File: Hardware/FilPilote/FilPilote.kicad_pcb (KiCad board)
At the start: 2 copper layers, 50 x 40 mm, 15 parts, among them J1 Conn_01x04_Male, P1 CONN_01X03, U1 MOC3041M, U2 MOC3041M, U4 ESP-12E, U5 HLK-PM03

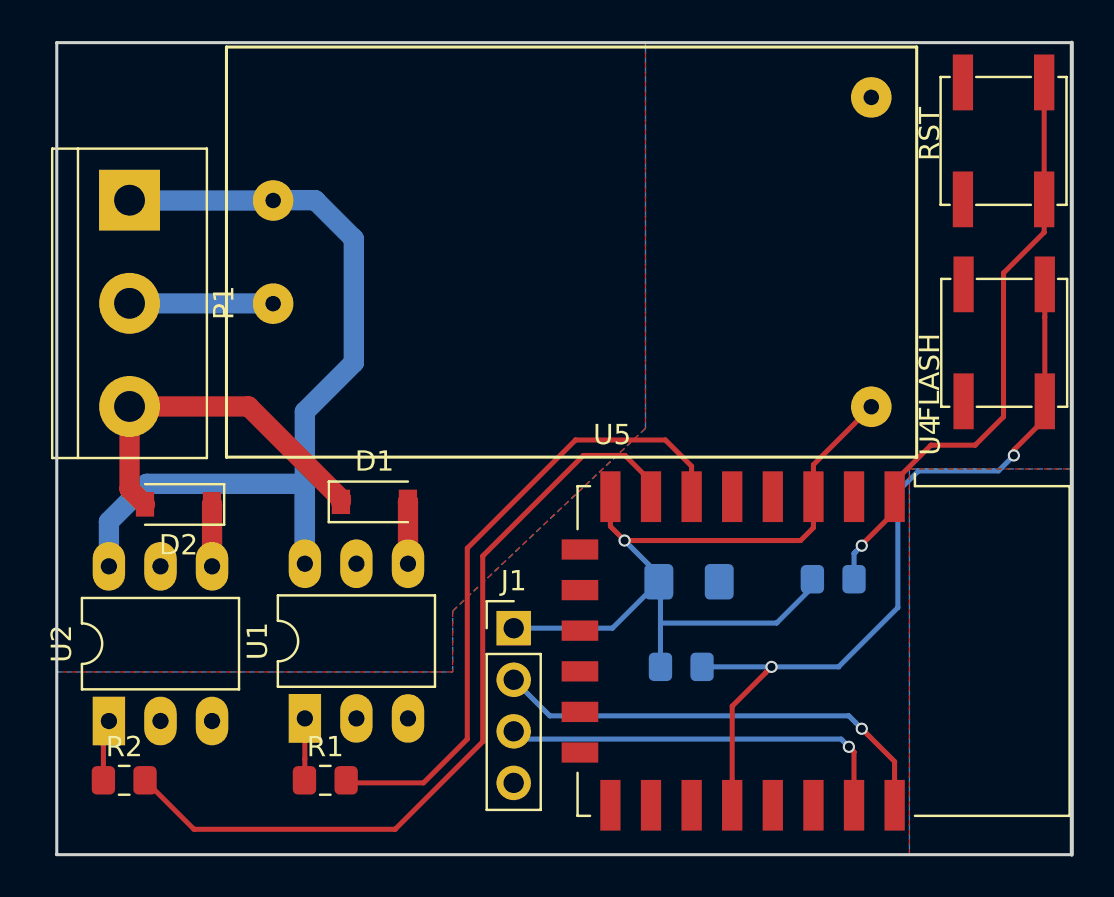
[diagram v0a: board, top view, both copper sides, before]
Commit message: - Modified almost all hardware boards : They were missing a pull-up resistor on GPIO2, which made impossible to flash. - Updated baseBoard.* files
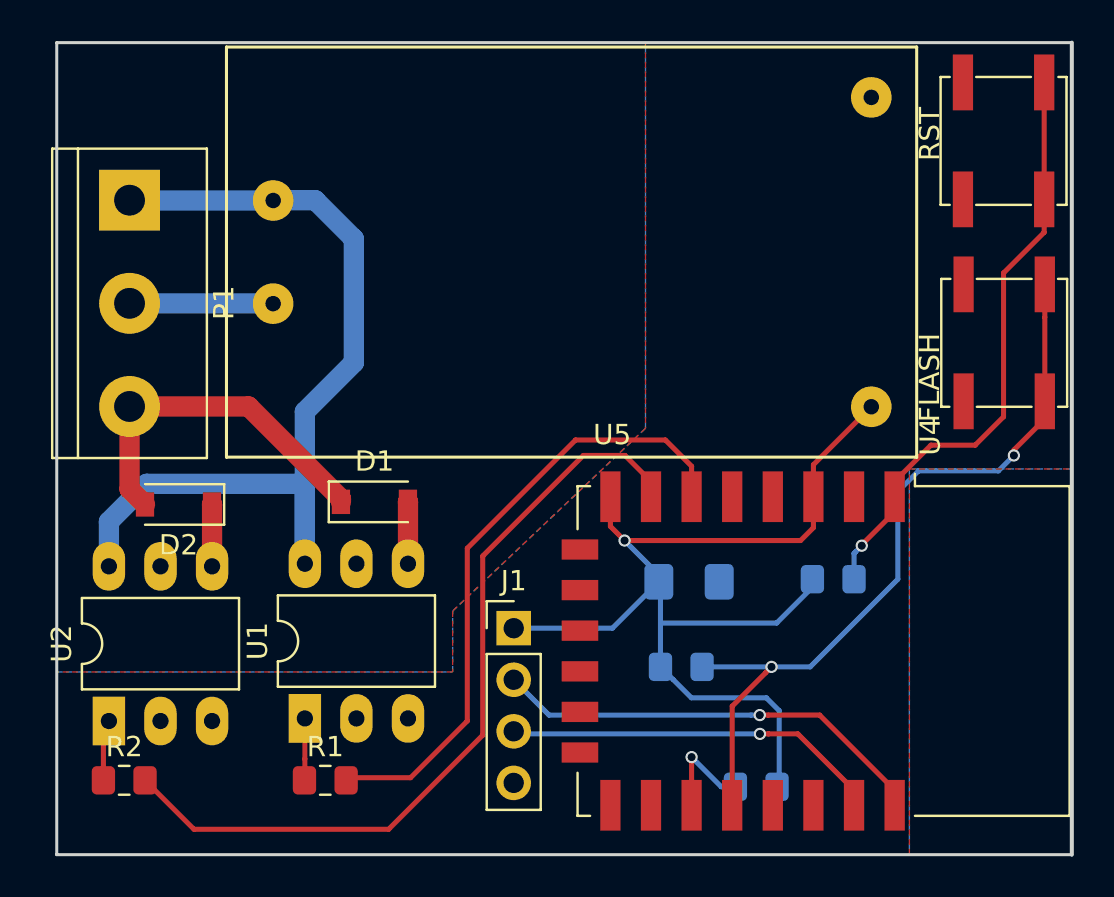
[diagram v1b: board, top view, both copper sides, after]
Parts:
- added R3: 10K, Resistor_SMD:R_0805_2012Metric_Pad1.15x1.40mm_HandSolder, B.Cu at (145.8, 109.0)
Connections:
- U4 pad 17: (no net) -> Net-(R3-Pad1)
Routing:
- net /3V3: track 42.8 -> 53.4 mm
- net Net-(R3-Pad1): track 0.00 -> 5.14 mm, vias 0 -> 1
- net /RXD: track 19.8 -> 18.7 mm
- net /TXD: track 22.6 -> 21.8 mm
- net Net-(R8-Pad1): track 39.7 -> 38.9 mm
- net /O1: track 31.7 -> 31.0 mm

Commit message: Fix on the BaseBoard class
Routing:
- net /3V3: track 53.4 -> 57.8 mm
- net /O1: track 31.0 -> 32.5 mm, vias 0 -> 2
- net /O2: track 40.0 -> 39.7 mm, vias 0 -> 2
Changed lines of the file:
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@@
     (thickness 1.6)
     (drawings 4)
-    (tracks 124)
+    (tracks 129)
     (zones 0)
     (modules 16)
@@
     (visible_elements FFFFFF7F)
     (pcbplotparams
-      (layerselection 0x010f0_80000001)
+      (layerselection 0x010f0_ffffffff)
       (usegerberextensions true)
       (usegerberattributes false)
@@
   (segment (start 148.572 98.806) (end 148.59 98.824) (width 0.25) (layer B.Cu) (net 2))
   (segment (start 148.59 98.824) (end 148.59 99.187) (width 0.25) (layer B.Cu) (net 2))
-  (segment (start 147.987 96.901) (end 139.319 96.901) (width 0.25) (layer F.Cu) (net 2))
-  (segment (start 148.622 94.742) (end 148.622 96.266) (width 0.25) (layer F.Cu) (net 2))
-  (segment (start 148.622 96.266) (end 147.987 96.901) (width 0.25) (layer F.Cu) (net 2))
   (segment (start 141.711372 103.747372) (end 141.088 103.124) (width 0.25) (layer B.Cu) (net 2))
   (segment (start 146.83 108.8845) (end 146.939 108.7755) (width 0.25) (layer B.Cu) (net 2))
@@
   (segment (start 146.939 105.283) (end 146.304 104.648) (width 0.25) (layer B.Cu) (net 2))
   (segment (start 142.612 104.648) (end 141.711372 103.747372) (width 0.25) (layer B.Cu) (net 2))
+  (segment (start 141.551999 90.312001) (end 150.058788 90.312001) (width 0.25) (layer F.Cu) (net 2))
+  (segment (start 150.058788 90.312001) (end 151.473001 90.312001) (width 0.25) (layer F.Cu) (net 2))
+  (segment (start 138.622 93.242) (end 141.551999 90.312001) (width 0.25) (layer F.Cu) (net 2))
+  (segment (start 138.622 94.742) (end 138.622 93.242) (width 0.25) (layer F.Cu) (net 2))
   (segment (start 128.651 94.998) (end 128.649 94.996) (width 1) (layer F.Cu) (net 3))
   (segment (start 128.651 98.044) (end 128.651 94.998) (width 1) (layer F.Cu) (net 3))
@@
   (segment (start 133.985 106.426) (end 145.986494 106.426) (width 0.25) (layer B.Cu) (net 11))
   (segment (start 125.748 108.585) (end 125.621 108.458) (width 0.25) (layer F.Cu) (net 12))
-  (segment (start 128.778 108.585) (end 125.748 108.585) (width 0.25) (layer F.Cu) (net 12))
-  (segment (start 142.622 93.242) (end 141.328 91.948) (width 0.25) (layer F.Cu) (net 12))
-  (segment (start 142.622 94.742) (end 142.622 93.242) (width 0.25) (layer F.Cu) (net 12))
-  (segment (start 141.328 91.948) (end 136.906 91.948) (width 0.25) (layer F.Cu) (net 12))
-  (segment (start 136.906 91.948) (end 131.572 97.282) (width 0.25) (layer F.Cu) (net 12))
-  (segment (start 131.572 97.282) (end 131.572 105.791) (width 0.25) (layer F.Cu) (net 12))
-  (segment (start 131.572 105.791) (end 128.778 108.585) (width 0.25) (layer F.Cu) (net 12))
-  (segment (start 118.11 111.125) (end 115.697 108.712) (width 0.25) (layer F.Cu) (net 13))
-  (segment (start 127.6985 111.125) (end 118.11 111.125) (width 0.25) (layer F.Cu) (net 13))
-  (segment (start 140.622 93.992) (end 139.34 92.71) (width 0.25) (layer F.Cu) (net 13))
-  (segment (start 140.622 94.742) (end 140.622 93.992) (width 0.25) (layer F.Cu) (net 13))
-  (segment (start 132.334 106.4895) (end 127.6985 111.125) (width 0.25) (layer F.Cu) (net 13))
-  (segment (start 139.34 92.71) (end 137.287 92.71) (width 0.25) (layer F.Cu) (net 13))
-  (segment (start 137.287 92.71) (end 132.334 97.663) (width 0.25) (layer F.Cu) (net 13))
-  (segment (start 132.334 97.663) (end 132.334 106.4895) (width 0.25) (layer F.Cu) (net 13))
+  (segment (start 142.622 94.742) (end 142.622 106.298) (width 0.25) (layer F.Cu) (net 12))
+  (via (at 141.605 107.315) (size 0.6) (drill 0.4) (layers F.Cu B.Cu) (net 12))
+  (segment (start 142.622 106.298) (end 141.605 107.315) (width 0.25) (layer F.Cu) (net 12))
+  (segment (start 141.605 107.315) (end 137.287 111.633) (width 0.25) (layer B.Cu) (net 12))
+  (via (at 127.889 111.506) (size 0.6) (drill 0.4) (layers F.Cu B.Cu) (net 12))
+  (segment (start 137.287 111.633) (end 128.016 111.633) (width 0.25) (layer B.Cu) (net 12))
+  (segment (start 128.016 111.633) (end 127.889 111.506) (width 0.25) (layer B.Cu) (net 12))
+  (segment (start 125.603 109.22) (end 125.603 108.712) (width 0.25) (layer F.Cu) (net 12))
+  (segment (start 127.889 111.506) (end 125.603 109.22) (width 0.25) (layer F.Cu) (net 12))
+  (via (at 125.603 110.998) (size 0.6) (drill 0.4) (layers F.Cu B.Cu) (net 13))
+  (segment (start 115.697 108.712) (end 117.983 110.998) (width 0.25) (layer F.Cu) (net 13))
+  (segment (start 117.983 110.998) (end 125.603 110.998) (width 0.25) (layer F.Cu) (net 13))
+  (via (at 140.081 107.315) (size 0.6) (drill 0.4) (layers F.Cu B.Cu) (net 13))
+  (segment (start 136.697999 110.698001) (end 140.081 107.315) (width 0.25) (layer B.Cu) (net 13))
+  (segment (start 125.603 110.998) (end 125.902999 110.698001) (width 0.25) (layer B.Cu) (net 13))
+  (segment (start 125.902999 110.698001) (end 136.697999 110.698001) (width 0.25) (layer B.Cu) (net 13))
+  (segment (start 140.622 97.376) (end 140.622 94.742) (width 0.25) (layer F.Cu) (net 13))
+  (segment (start 140.081 107.315) (end 140.622 106.774) (width 0.25) (layer F.Cu) (net 13))
+  (segment (start 140.622 106.774) (end 140.622 97.376) (width 0.25) (layer F.Cu) (net 13))
   (segment (start 159.988 74.336) (end 159.988 80.096) (width 0.25) (layer F.Cu) (net 14))
   (segment (start 152.622 93.992) (end 152.622 94.742) (width 0.25) (layer F.Cu) (net 14))
@@
       (pts
         (xy 161.35 93.375) (xy 153.35 93.375) (xy 153.35 112.375) (xy 111.35 112.375) (xy 111.35 103.375)
-        (xy 130.85 103.375) (xy 130.85 100.375) (xy 140.35 91.375) (xy 140.35 72.375) (xy 161.35 72.375)
+        (xy 135.35 103.375) (xy 135.35 93.375) (xy 140.35 88.375) (xy 140.35 72.375) (xy 161.35 72.375)
       )
     )
@@
     (polygon
       (pts
-        (xy 161.35 72.375) (xy 140.35 72.375) (xy 140.35 91.375) (xy 130.85 100.375) (xy 130.85 103.375)
+        (xy 161.35 72.375) (xy 140.35 72.375) (xy 140.35 88.375) (xy 135.35 93.375) (xy 135.35 103.375)
         (xy 111.35 103.375) (xy 111.35 112.375) (xy 153.35 112.375) (xy 153.35 93.375) (xy 161.35 93.375)
       )
